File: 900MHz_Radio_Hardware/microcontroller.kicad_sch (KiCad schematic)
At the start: 1 part, among them U2 Teensy4.1_DEV-16771

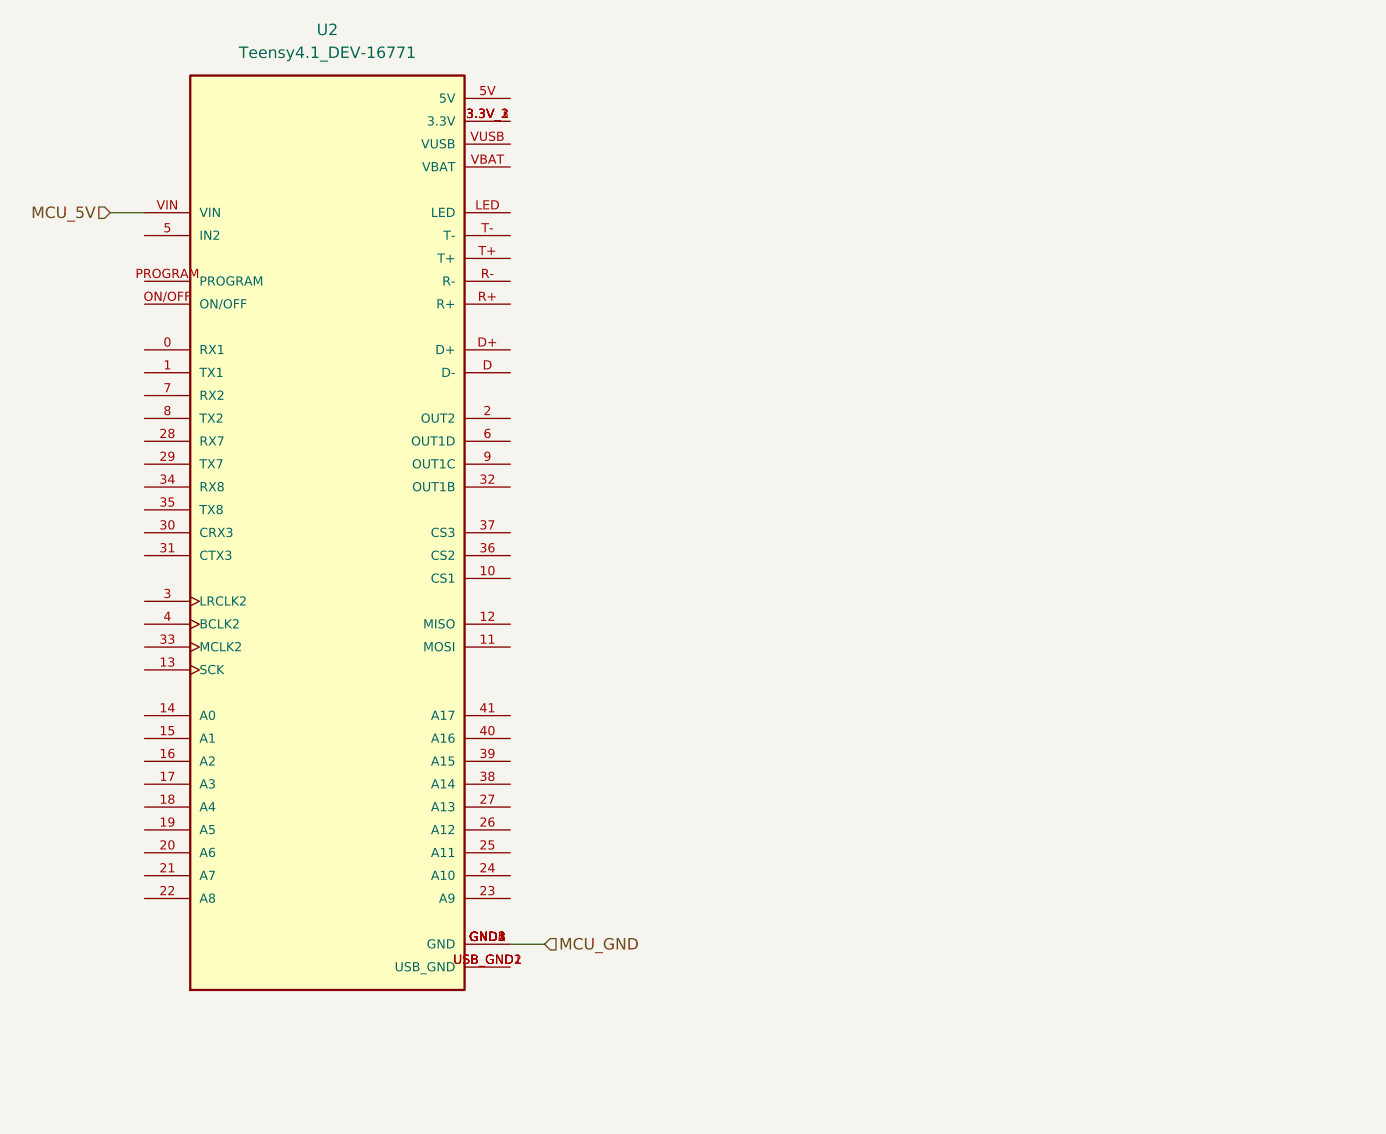
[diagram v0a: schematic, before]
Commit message: Replaced oscillator
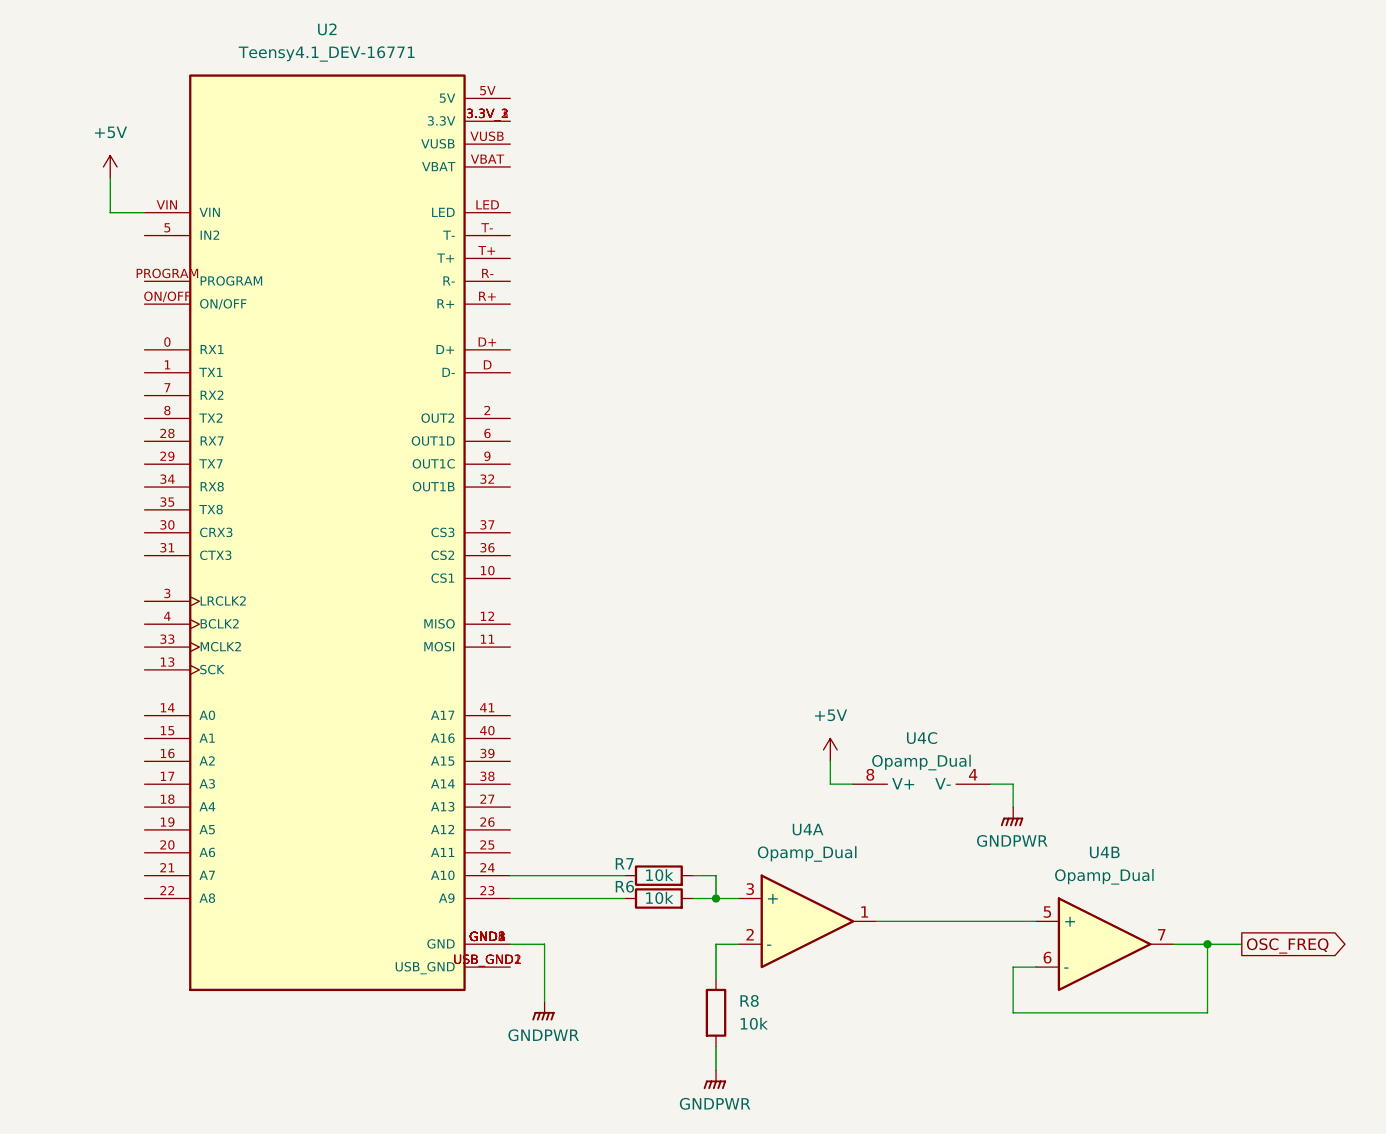
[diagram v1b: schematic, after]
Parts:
- added R6, R7, R8: 10k, symbol Device:R
- added U4: Opamp_Dual, symbol Device:Opamp_Dual
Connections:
- net at U2.23 (A9): now also R6.1
- net at U2.24 (A10): now also R7.1
- net MCU_5V renamed +5V
- net +5V: now also U4.8 (V+)
- net MCU_GND renamed GNDPWR
- net GNDPWR: now also R8.2, U4.4 (V-)
- new net: U4.1, U4.5 (+)
- new net: R6.2, R7.2, U4.3 (+)
- new net: R8.1, U4.2 (-)
- new net OSC_FREQ: U4.6 (-), U4.7

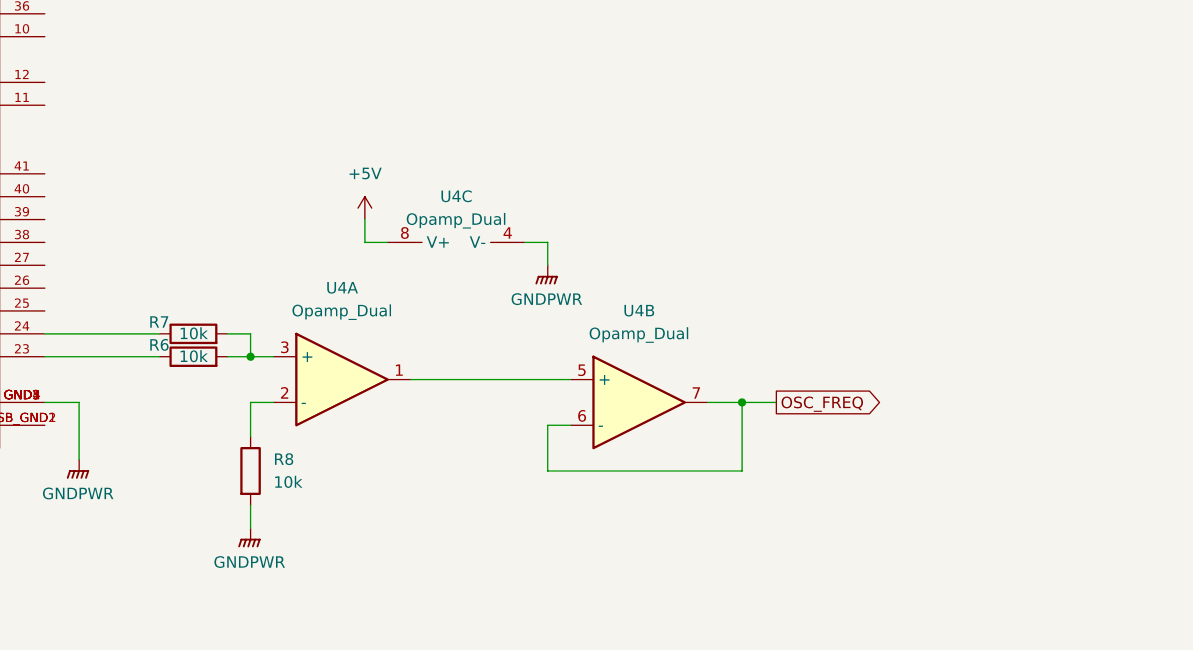
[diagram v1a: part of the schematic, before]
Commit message: Oscillator control circuit
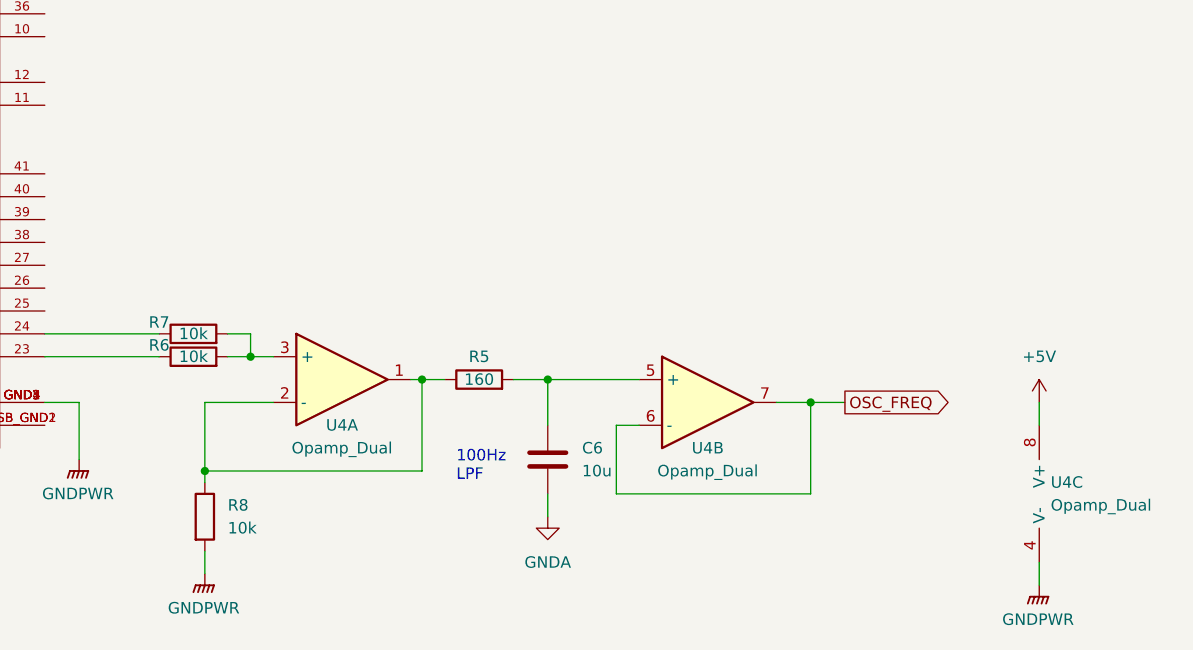
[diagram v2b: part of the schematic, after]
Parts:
- added C6: 10u, symbol Device:C
- added R5: 160, symbol Device:R
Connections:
- net at U4.5 (+): now also C6.1, R5.2; no longer U4.1
- net at R8.1, U4.2 (-): now also U4.1, R5.1
- new net GNDA: C6.2
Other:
- note added: "100Hz LPF"
- moved on the sheet: R8, U4B, U4C

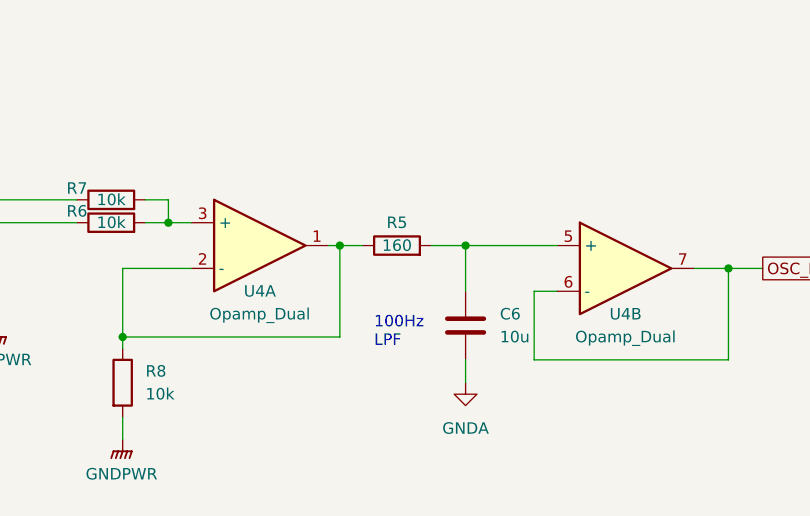
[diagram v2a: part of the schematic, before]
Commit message: Adjusted filter cutoff
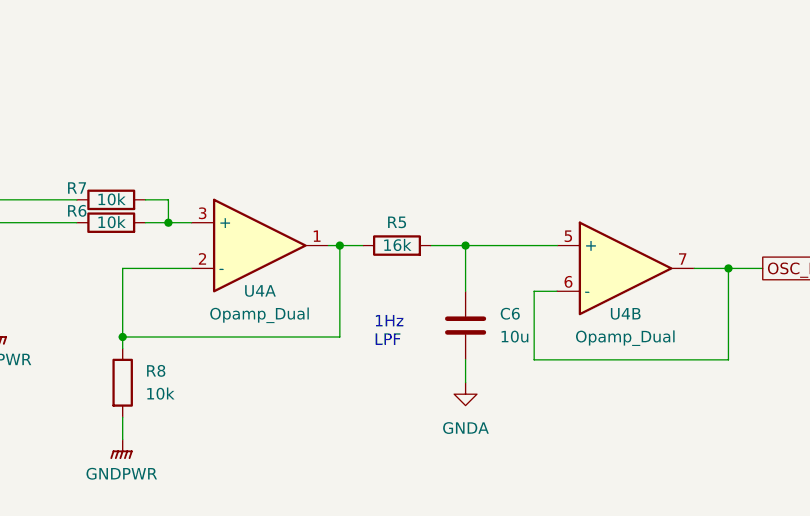
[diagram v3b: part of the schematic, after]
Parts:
- R5: value 160 -> 16k
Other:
- note added: "1Hz LPF"
- note removed: "100Hz LPF"
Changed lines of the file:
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@@
     (stroke (width 0) (type default))
   )
-  (text "100Hz\nLPF" (at 213.36 147.32 0)
+  (text "1Hz\nLPF" (at 213.36 147.32 0)
     (effects (font (size 1.27 1.27)) (justify left bottom))
   )
@@
       (effects (font (size 1.27 1.27)))
     )
-    (property "Value" "160" (at 215.9 135.89 90)
-      (effects (font (size 1.27 1.27)))
-    )
+    (property "Value" "16k" (at 215.9 135.89 90)
+      (effects (font (size 1.27 1.27)))
+    )

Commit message: Updated filter
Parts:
- removed C6: 10u, symbol Device:C
- removed R5: 16k, symbol Device:R
- removed R6, R7, R8: 10k, symbol Device:R
- removed U4: Opamp_Dual, symbol Device:Opamp_Dual
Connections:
- net OSC_CTL_B: now reaches U2.24 (A10)
- net OSC_CTL_A: now reaches U2.23 (A9)
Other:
- note removed: "1Hz LPF"

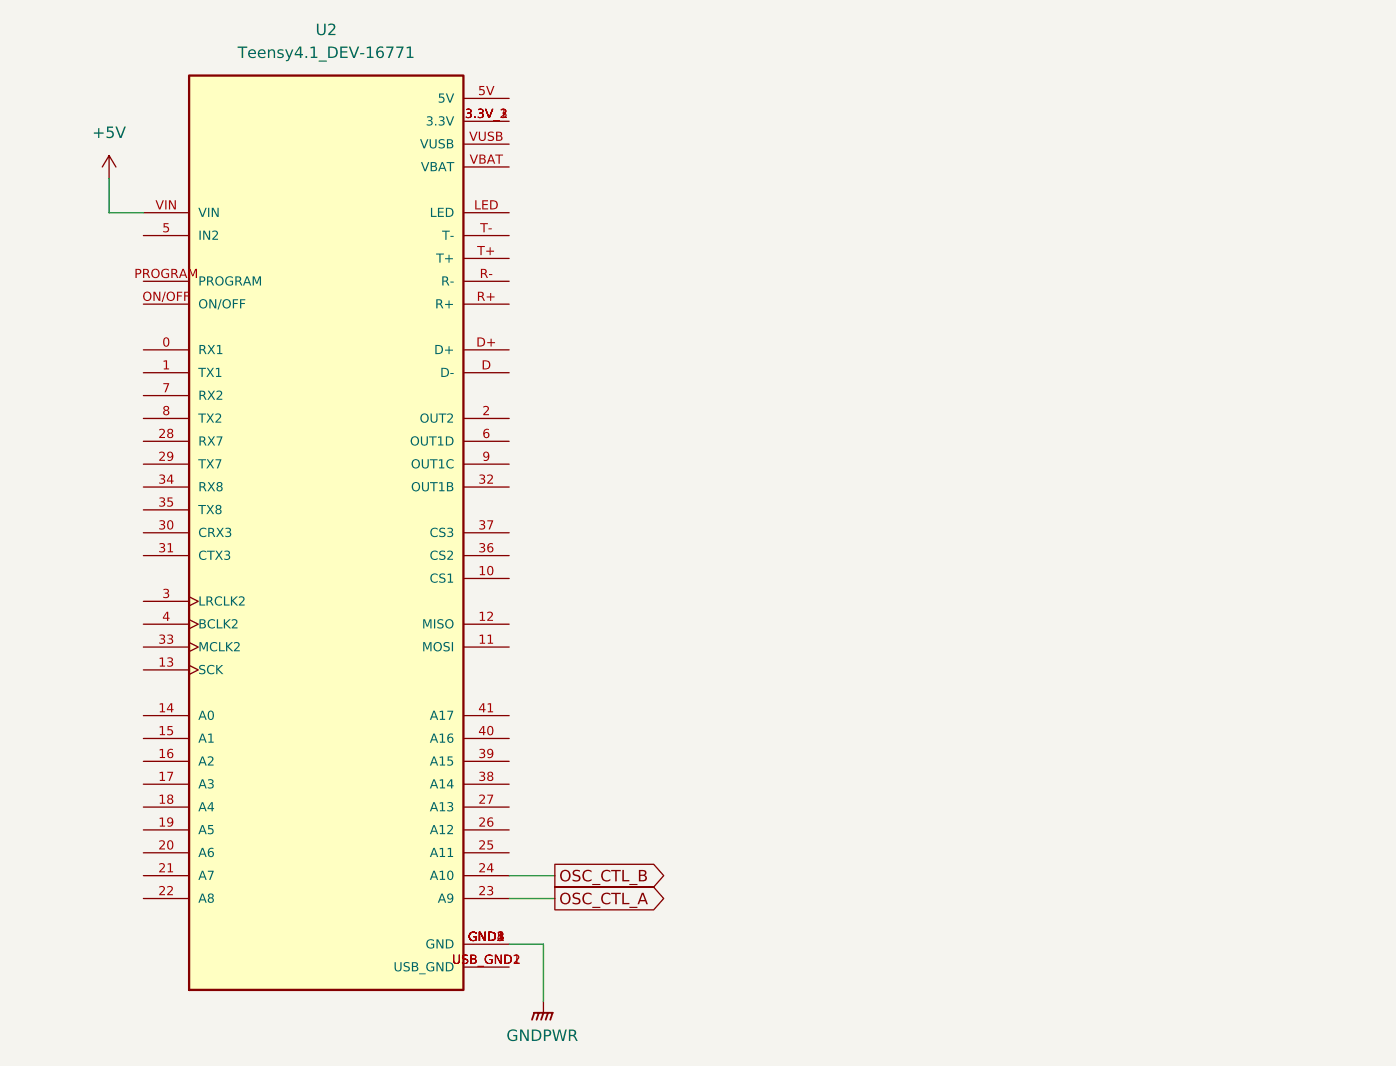
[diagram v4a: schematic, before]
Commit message: Completed oscillator
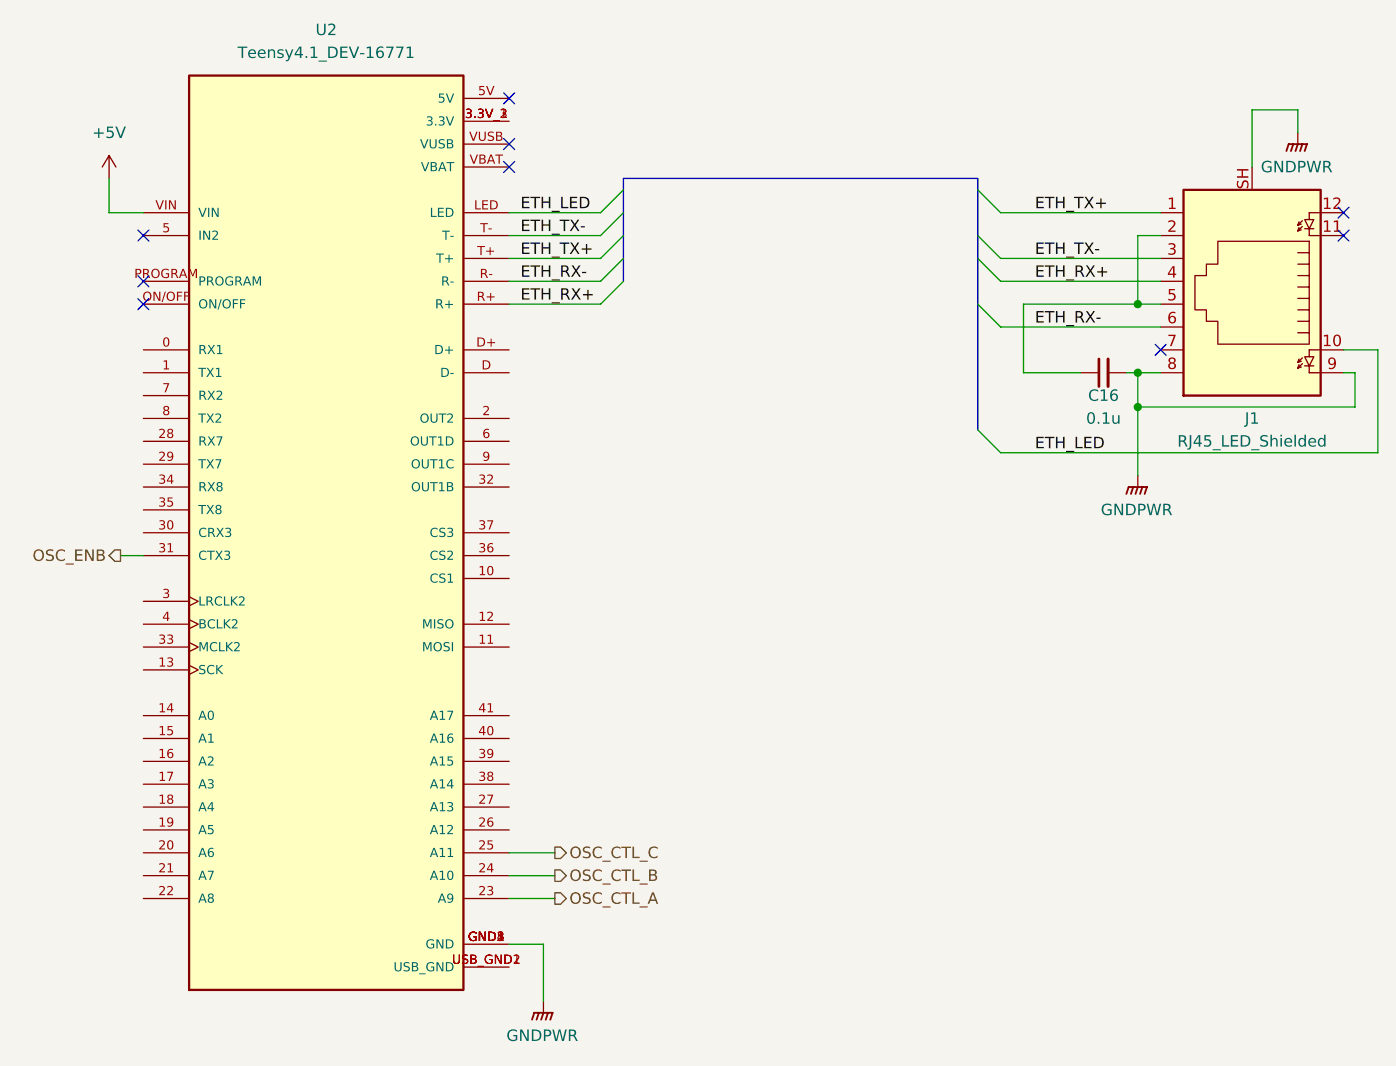
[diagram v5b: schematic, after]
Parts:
- added C16: 0.1u, symbol Device:C_Small
- added J1: RJ45_LED_Shielded, symbol Connector:RJ45_LED_Shielded
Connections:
- net GNDPWR: now also C16.2, J1.8, J1.9, J1.SH
- net OSC_CTL_C: now reaches U2.25 (A11)
- net OSC_ENB: now reaches U2.31 (CTX3)
- net ETH_LED: now reaches U2.LED
- net ETH_LED: now also J1.10
- net ETH_RX+: now reaches U2.R+
- net ETH_RX+: now also J1.4
- net ETH_RX-: now reaches U2.R-
- net ETH_RX-: now also J1.6
- net ETH_TX+: now reaches U2.T+
- net ETH_TX+: now also J1.1
- net ETH_TX-: now reaches U2.T-
- net ETH_TX-: now also J1.3
- new net: C16.1, J1.2, J1.5
- no-connect marks 0 -> 9
